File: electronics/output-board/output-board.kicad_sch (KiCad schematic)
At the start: 33 parts, among them J14 Arming switch, J19 Extra IO, J3 12V In, J4 Conn_01x02, J5 SWD Header, J6 Conn_01x02, SW1 SW_Push_Dual, U1 MAX33012EASA+, U2 LD3985M33R_SOT23, U3 STM32F105VBH6, Y1 25MHz 9pF

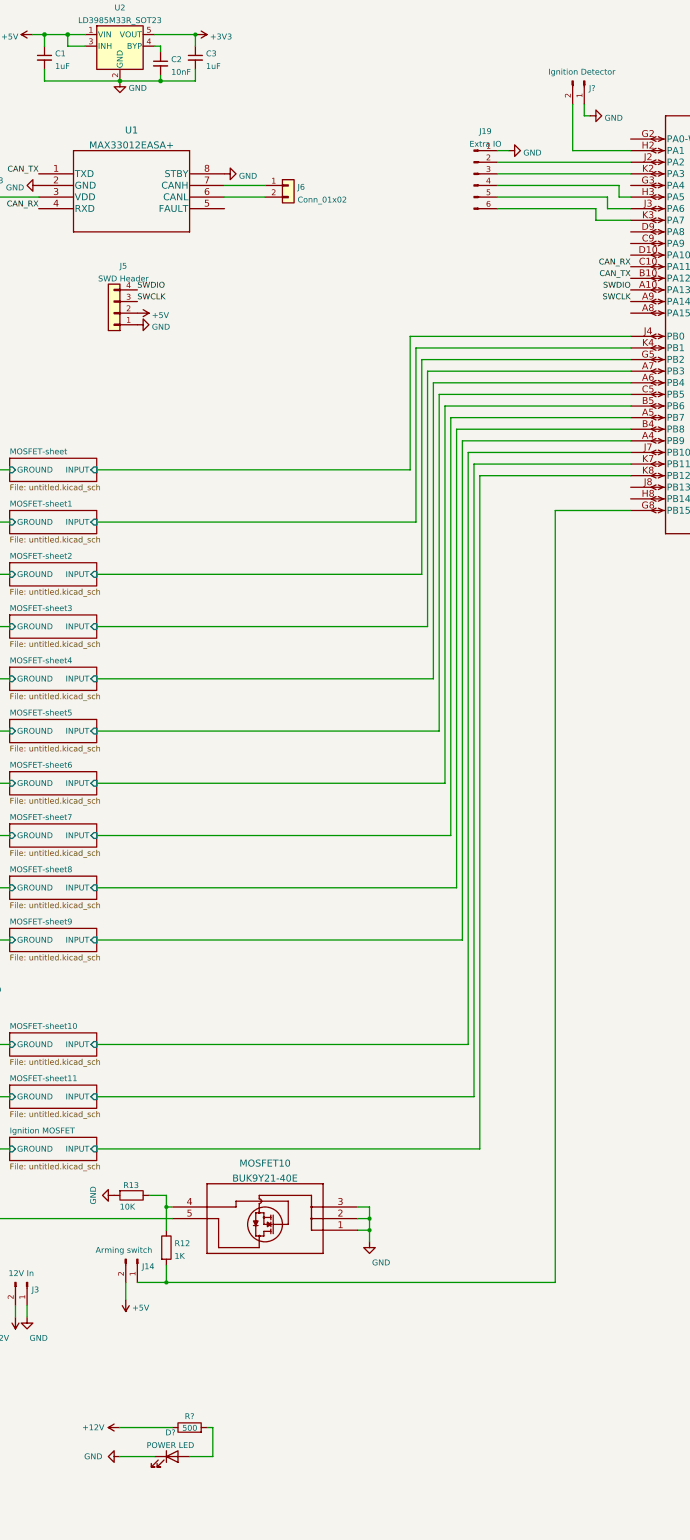
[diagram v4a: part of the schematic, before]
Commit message: added power leds and ignition detection
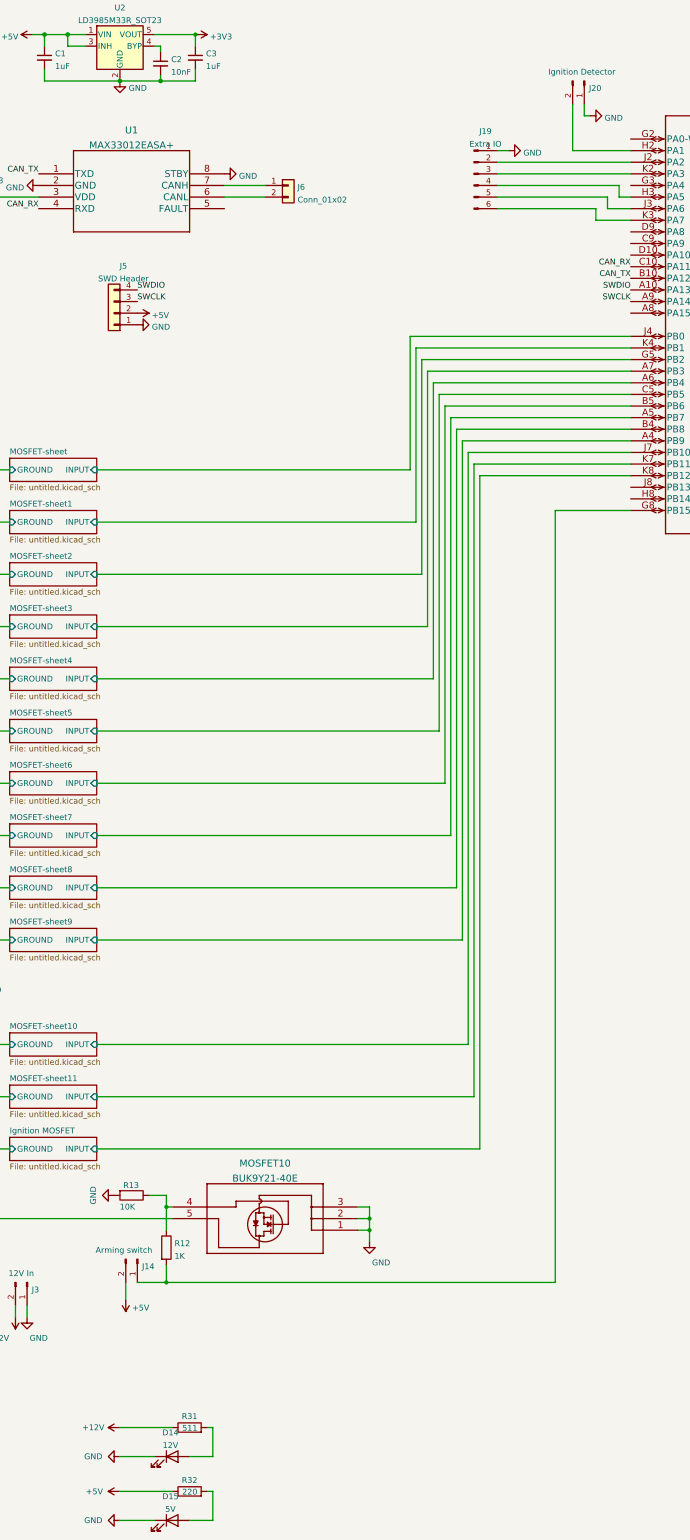
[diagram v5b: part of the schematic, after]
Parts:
- added D15: 5V, LED_SMD:LED_1206_3216Metric, symbol Device:LED
- added R32: 220, Resistor_SMD:R_0603_1608Metric, symbol Device:R
- D14: renamed from D?; value POWER LED -> 12V
- J20: renamed from J?; footprint CustomFootprints:PowerPoleThroughHole -> CustomFootprints:LatchingConnector2POS
- R31: renamed from R?; value 500 -> 511
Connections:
- net +5V: now also R32.1
- net GND: now also D15.1 (K)
- new net: D15.2 (A), R32.2

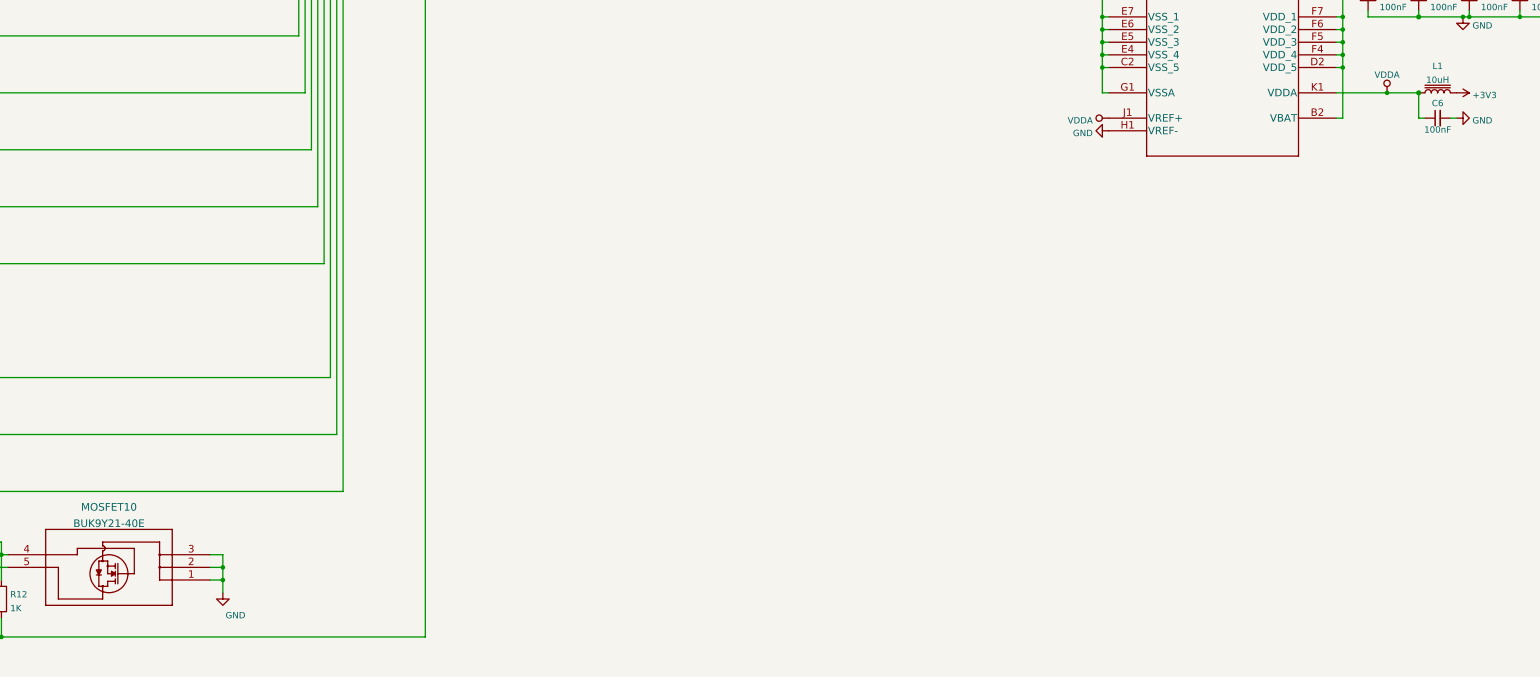
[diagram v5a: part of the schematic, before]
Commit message: Added test cases for output board
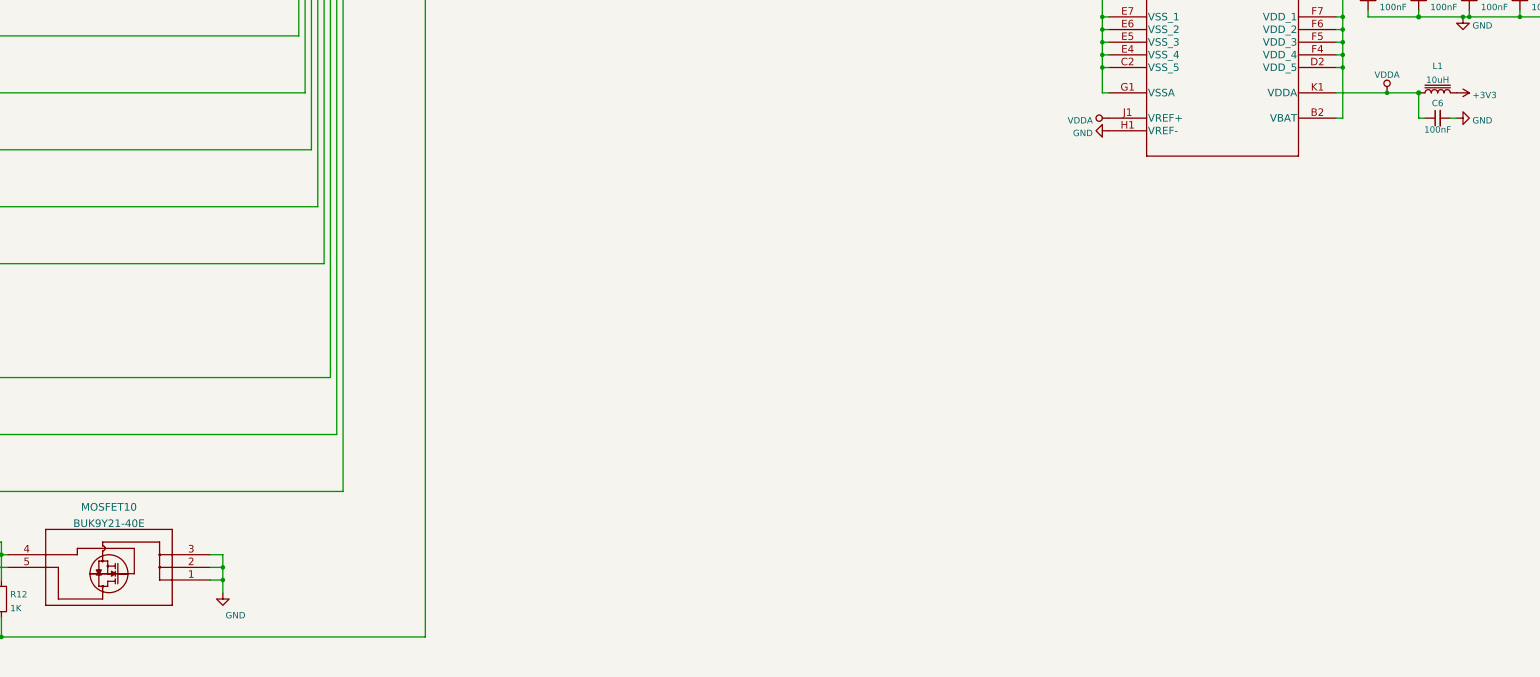
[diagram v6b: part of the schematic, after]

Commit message: Started updating the output board
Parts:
- added D?: LED, LED_SMD:LED_1206_3216Metric, symbol Device:LED
- added D?: 1N4007, Diode_THT:D_DO-41_SOD81_P10.16mm_Horizontal, symbol Diode:1N4007
- added J?: Conn_01x02_Male, CustomFootprints:LatchingConnector2POS, symbol Connector:Conn_01x02_Male
- added MOSFET?: BUK9Y21-40E, MOSFET 2:BUK9Y21-40E, symbol ArmingMOSFET:BUK9Y21-40E
- added R?: 1K, Resistor_SMD:R_0603_1608Metric, symbol Device:R
- added R?: 511, Resistor_SMD:R_0603_1608Metric, symbol Device:R
- Y1: value 25MHz 9pF -> 36MHz 9pF
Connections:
- net +12V: now also J?.2 (Pin_2), R?.1
- net +5V: now also D?.2 (A); no longer C1.1, U2.1 (VIN), U2.3 (INH)
- net at R12.1, R13.1: now also J14.1 (Pin_1), U3.G8 (PB15); no longer MOSFET10.4
- net Ignition MOSFET/GROUND renamed MOSFET-sheet10/GROUND
- net MOSFET-sheet10/GROUND: now also MOSFET?.1, MOSFET?.2, MOSFET?.3
- net Ignition MOSFET/INPUT: no longer names the net of U3.K8 (PB12)
- net Ignition MOSFET/INPUT: now also R?.1
- new net: MOSFET10.4, R12.2
- new net: MOSFET?.4, R?.2
- new net: C1.1, D?.1 (K), U2.1 (VIN), U2.3 (INH)
- new net: D?.2 (A), R?.2
- new net: D?.1 (K), J?.1 (Pin_1), MOSFET?.5
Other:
- removed sheet Ignition MOSFET
- note added: "Arming Switch"
- note added: "Igniter Cicuit"
- note added: "Power LEDs"
- moved on the sheet: D14, D15, MOSFET10, R12, R31, R32

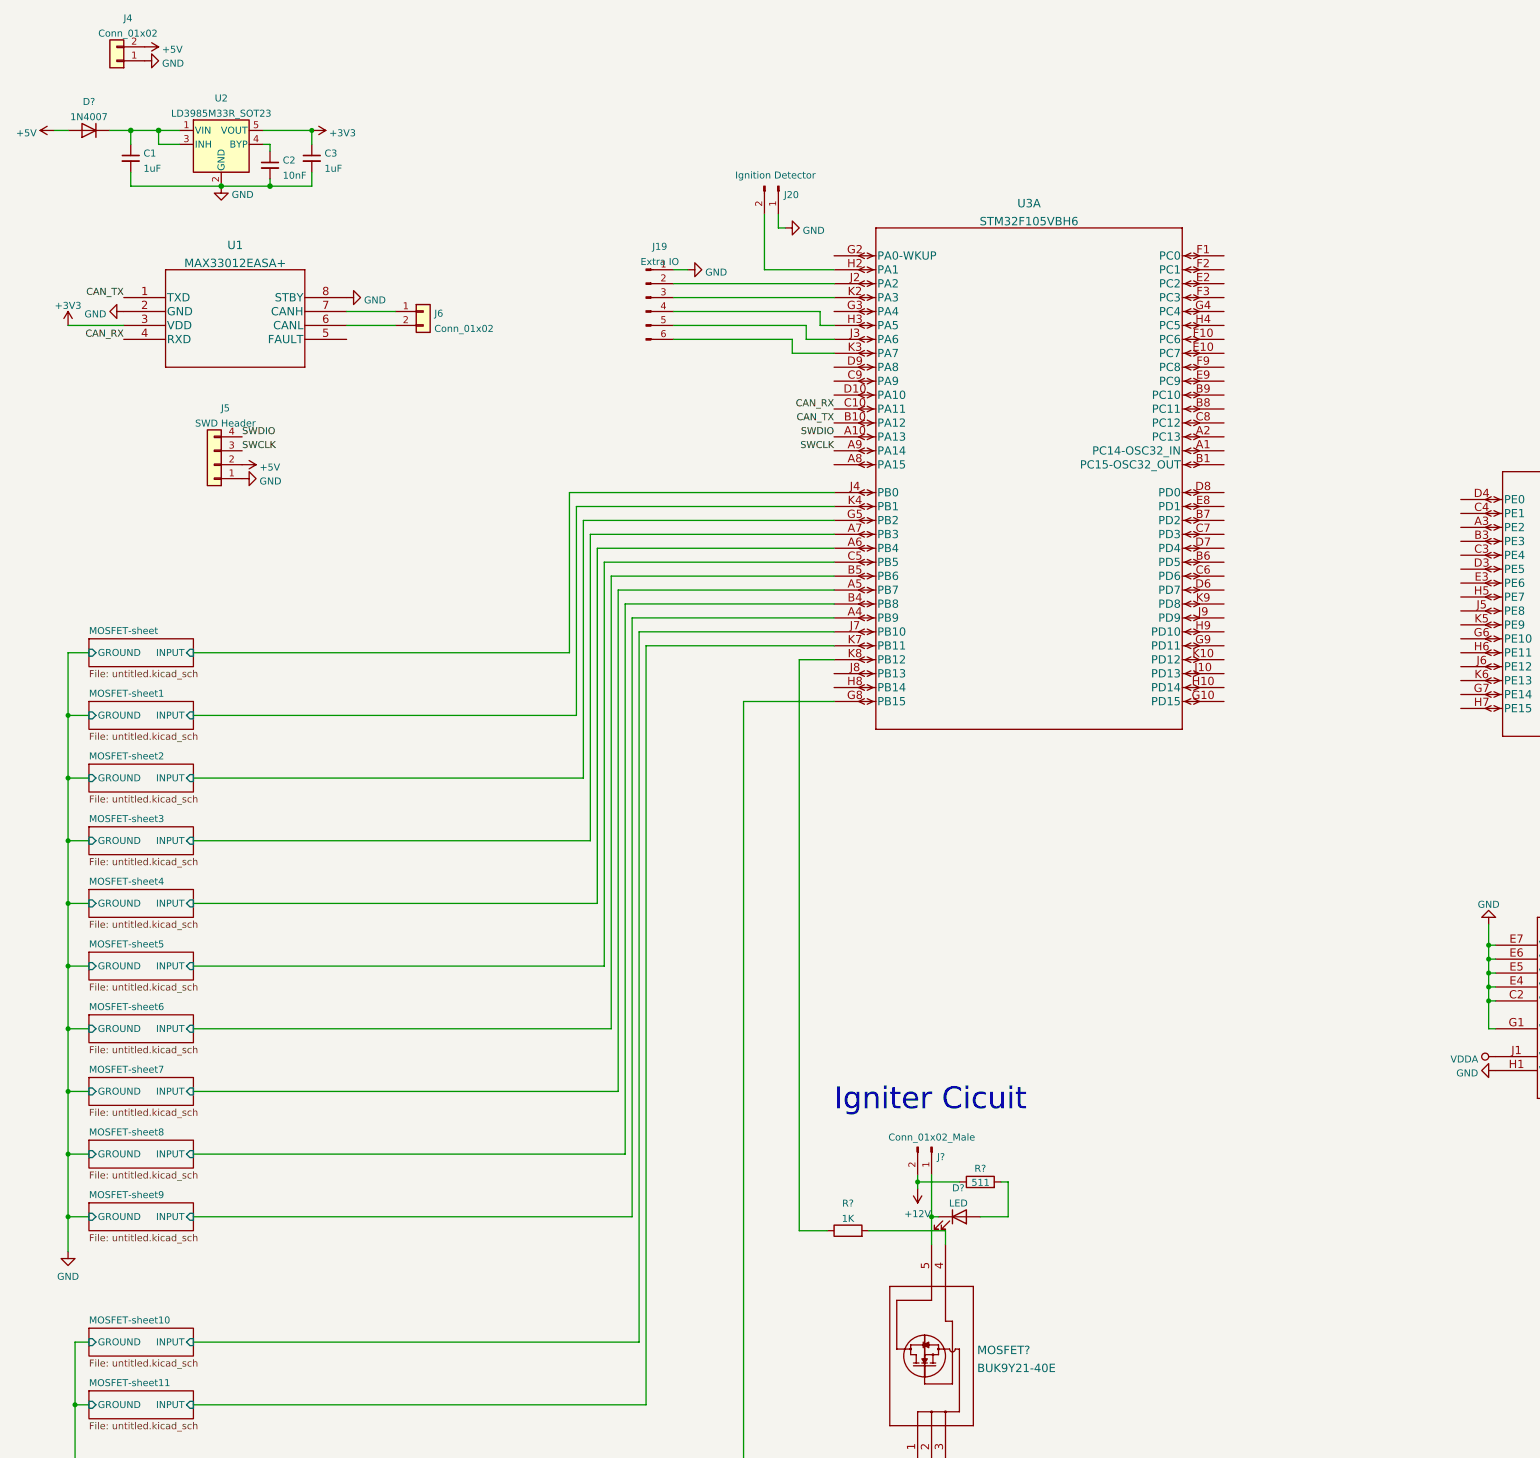
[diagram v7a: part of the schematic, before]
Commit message: Revising Output Board
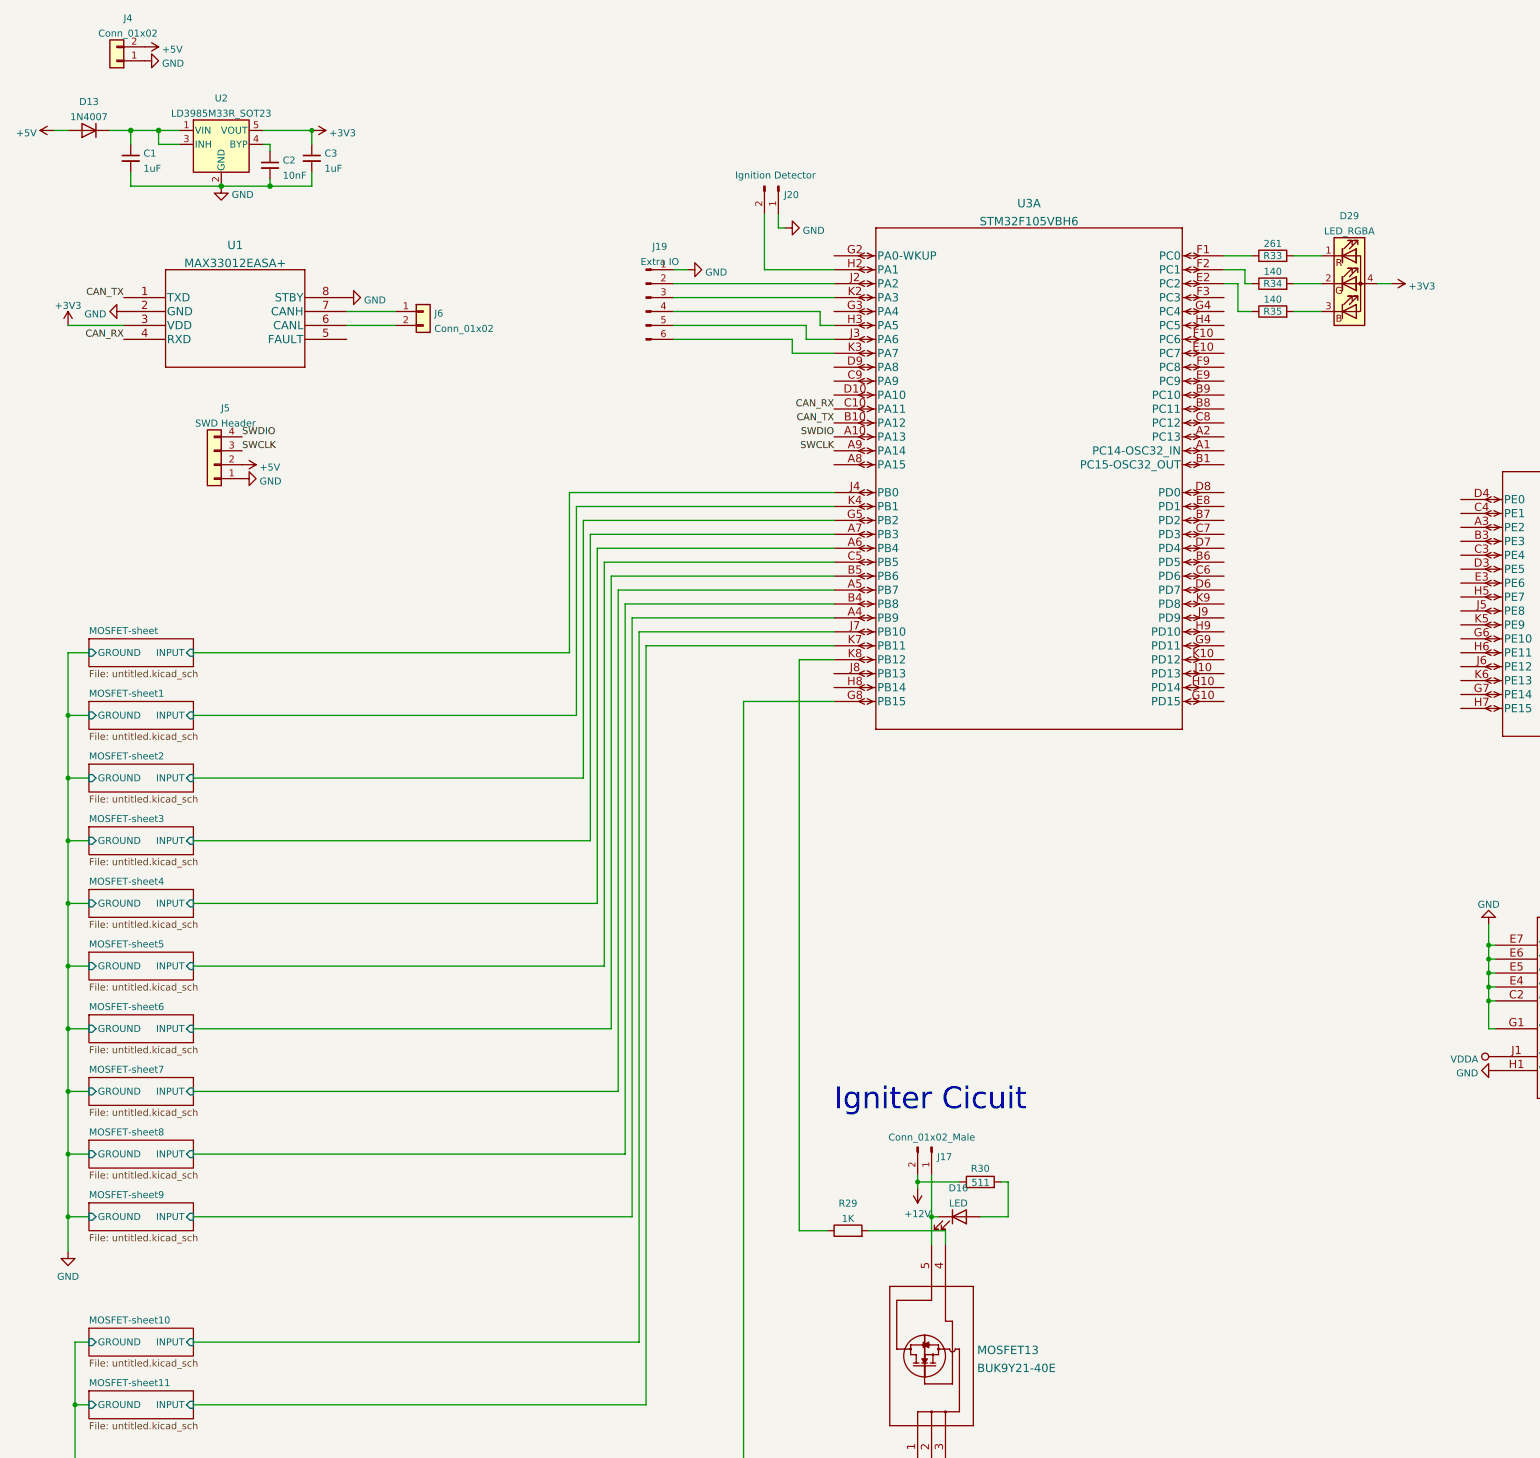
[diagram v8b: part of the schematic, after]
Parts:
- added D29: LED_RGBA, CustomFootprints:RGB LED, symbol Device:LED_RGBA
- added R33: 261, Resistor_SMD:R_0603_1608Metric, symbol Device:R
- added R34, R35: 140, Resistor_SMD:R_0603_1608Metric, symbol Device:R
- D13: renamed from D?; footprint Diode_THT:D_DO-41_SOD81_P10.16mm_Horizontal -> Diode_SMD:D_1206_3216Metric
- gave numbers to parts that had none: 5
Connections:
- net +3V3: now also D29.4 (A)
- net at U3.E2 (PC2): now also R35.1
- net at U3.F1 (PC0): now also R33.1
- net at U3.F2 (PC1): now also R34.1
- new net: D29.2 (GK), R34.2
- new net: D29.1 (RK), R33.2
- new net: D29.3 (BK), R35.2
